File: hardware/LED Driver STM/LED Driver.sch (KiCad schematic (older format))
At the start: 3 parts

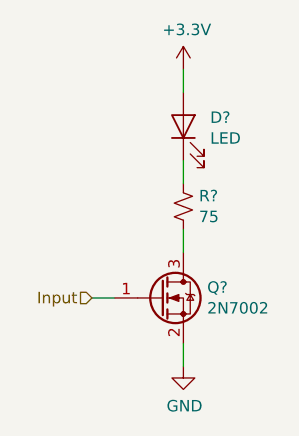
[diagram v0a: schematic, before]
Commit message: Updated layout
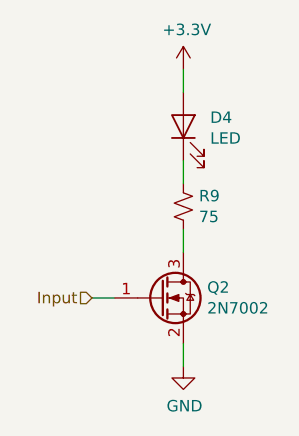
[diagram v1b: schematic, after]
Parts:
- gave numbers to parts that had none: 3
